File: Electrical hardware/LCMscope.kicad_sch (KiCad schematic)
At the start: 3 parts, among them U1 ICE40UP5K-SG48ITR, U2 LTC2299xUP, Y1 ASV-xxxMHz

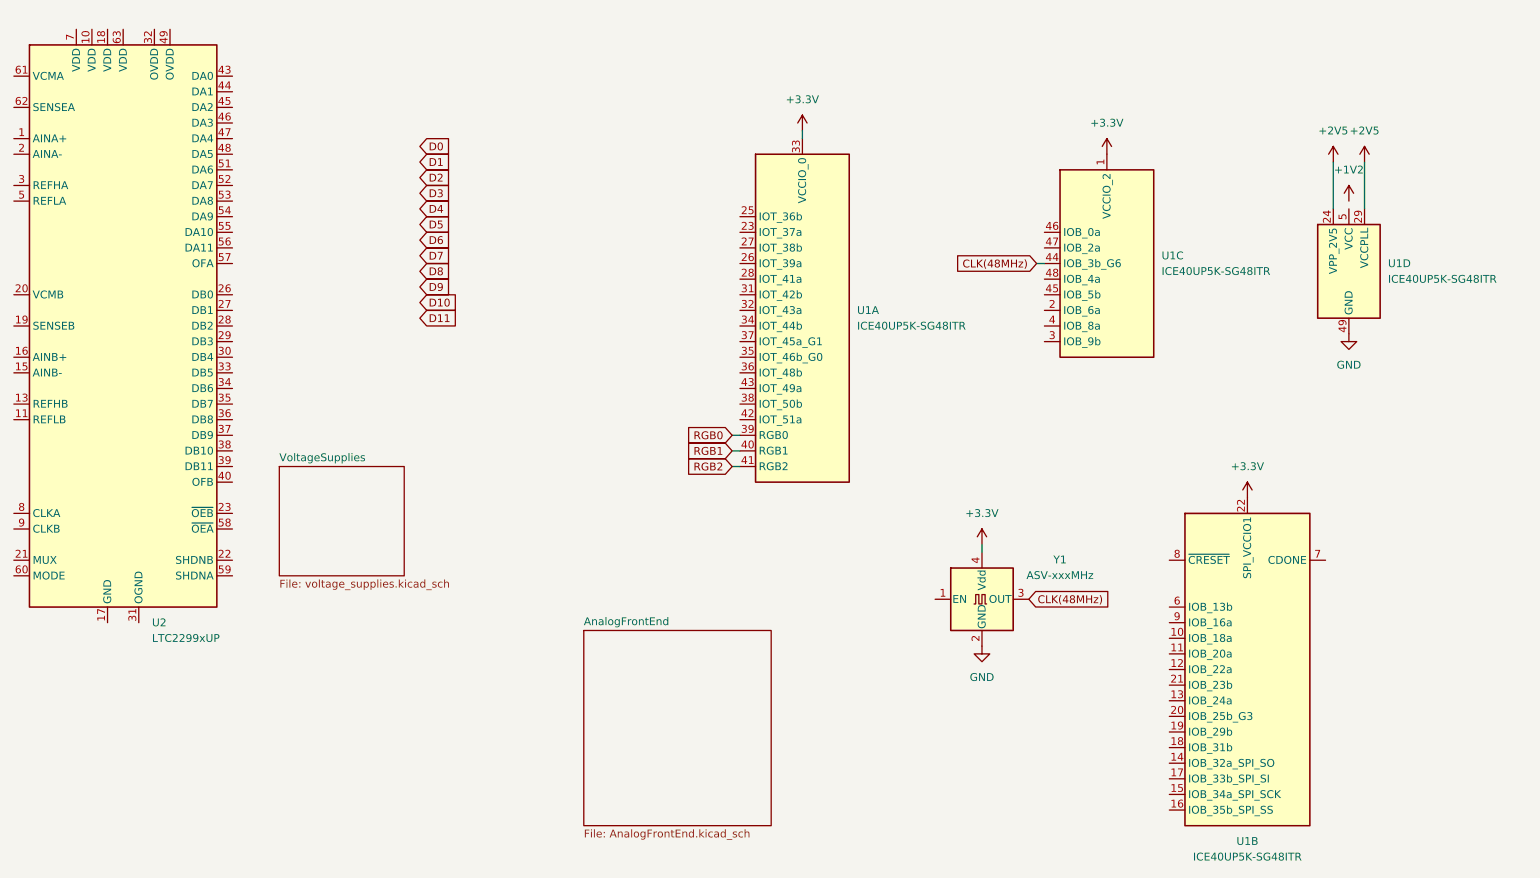
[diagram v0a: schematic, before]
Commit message: added hierarchical structure
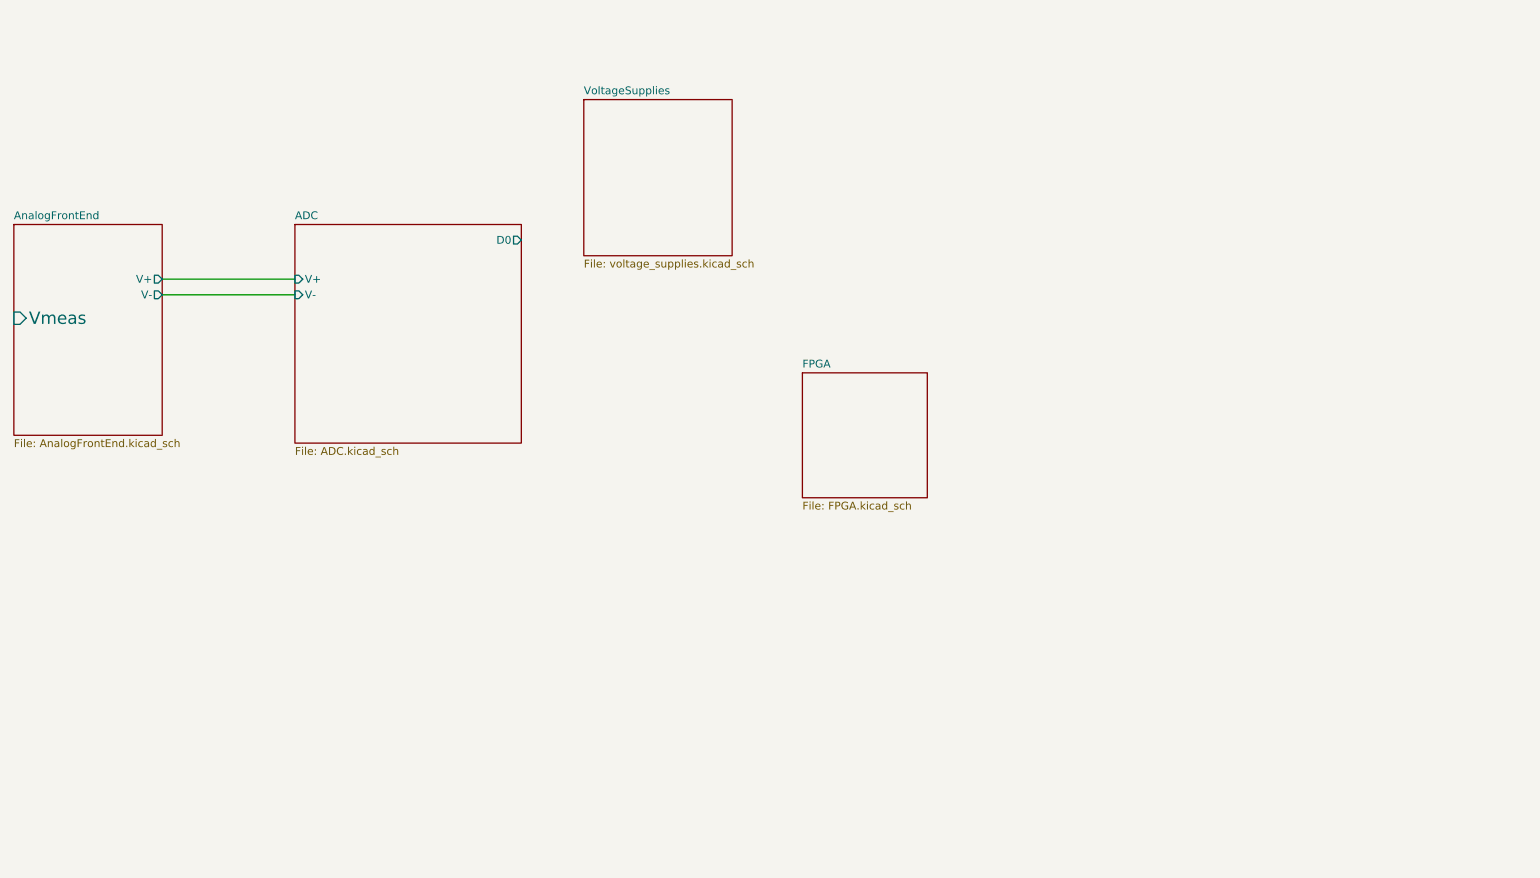
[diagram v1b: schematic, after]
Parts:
- removed U1: ICE40UP5K-SG48ITR, Package_DFN_QFN:QFN-48-1EP_7x7mm_P0.5mm_EP5.6x5.6mm, symbol FPGA_Lattice:ICE40UP5K-SG48ITR
- removed U2: LTC2299xUP, Package_DFN_QFN:QFN-64-1EP_9x9mm_P0.5mm_EP7.15x7.15mm, symbol Analog_ADC:LTC2299xUP
- removed Y1: ASV-xxxMHz, Oscillator:Oscillator_SMD_Abracon_ASV-4Pin_7.0x5.1mm, symbol Oscillator:ASV-xxxMHz
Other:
- added sheet ADC (ADC.kicad_sch)
- added sheet FPGA (FPGA.kicad_sch)
- sheet AnalogFrontEnd ports: added V+, V-, Vmeas; removed none

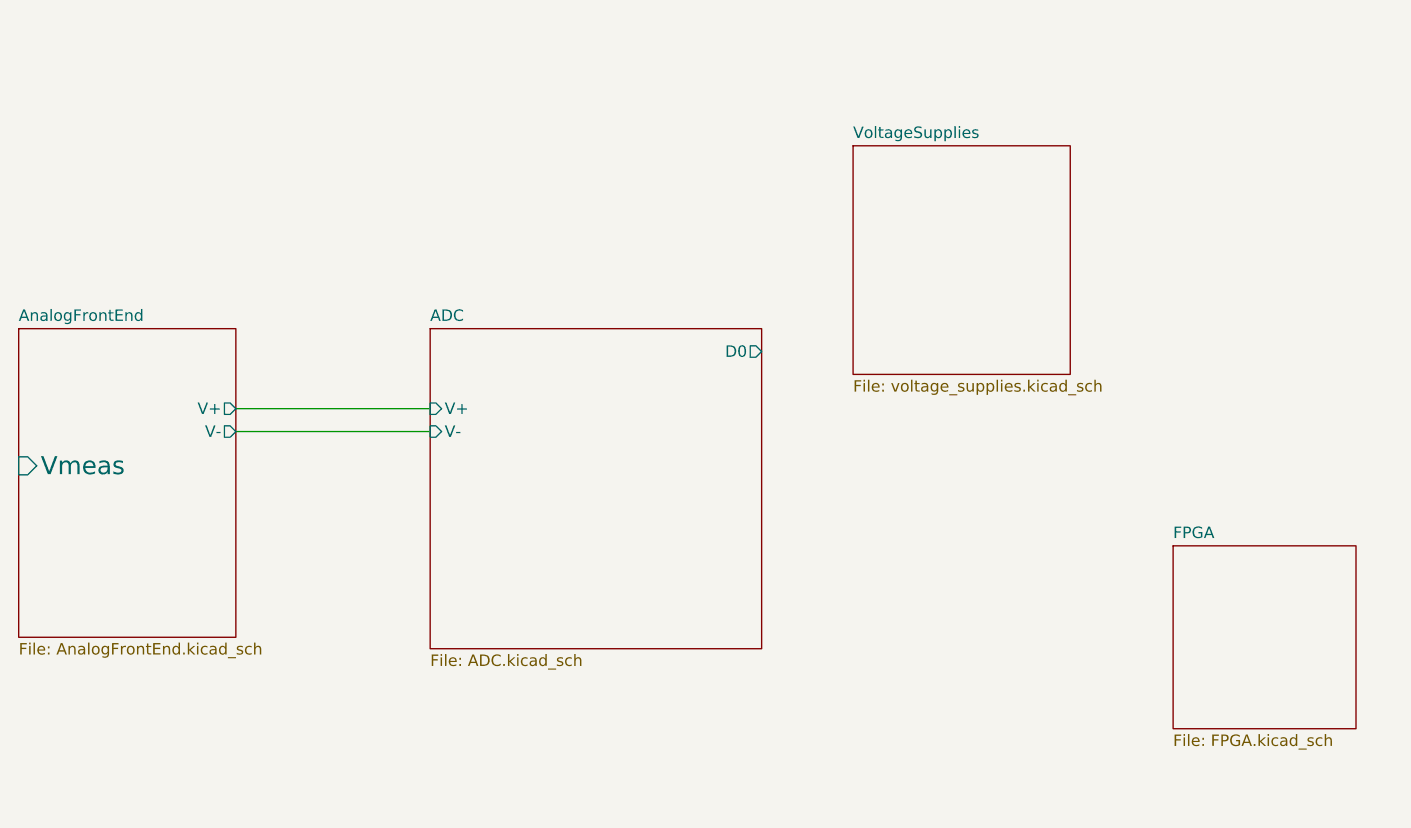
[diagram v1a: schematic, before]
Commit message: Created ADC footprint and extracted most important data from the data sheet
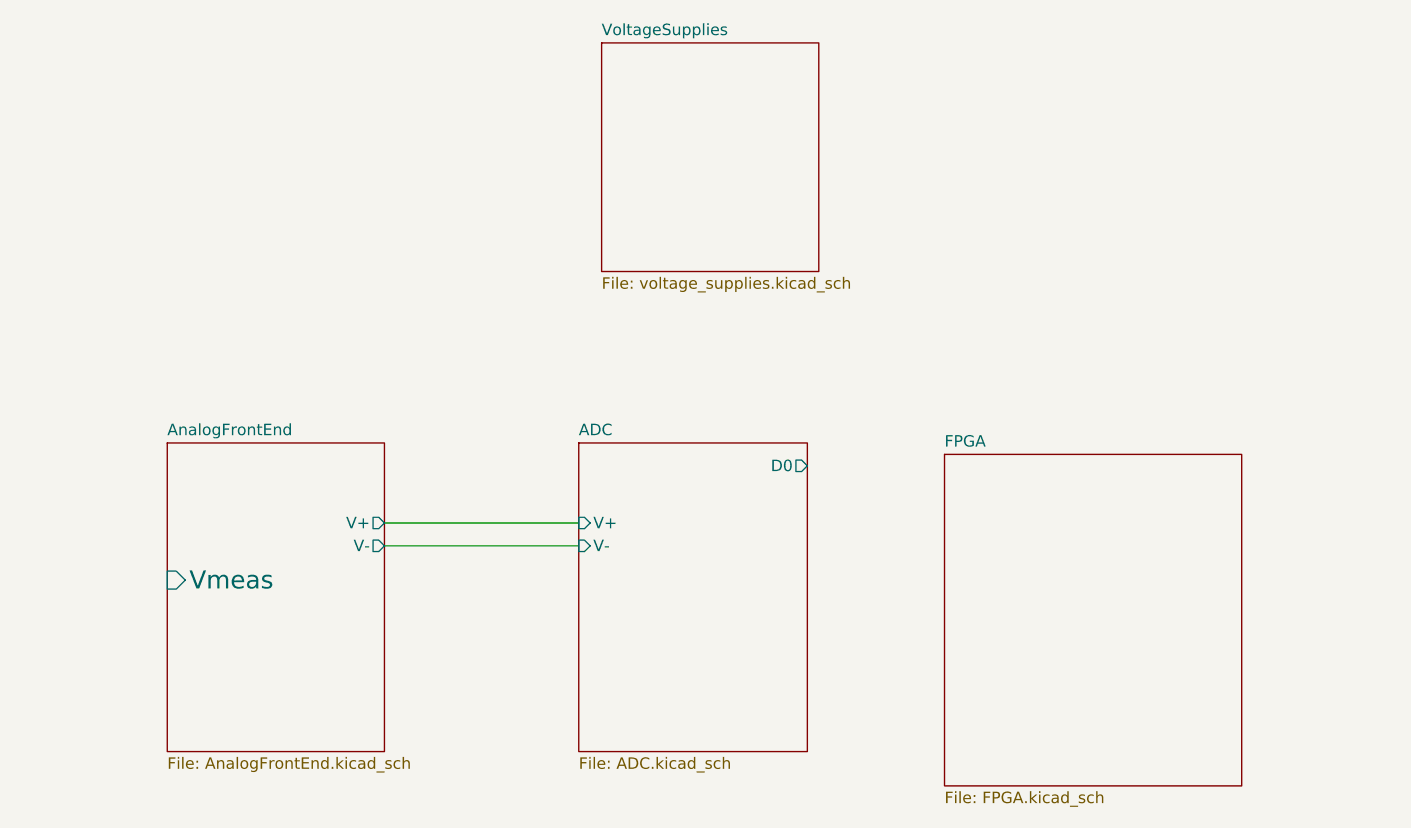
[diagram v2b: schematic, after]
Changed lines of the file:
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@@
 	(wire
 		(pts
-			(xy 64.77 55.88) (xy 86.36 55.88)
+			(xy 81.28 68.58) (xy 102.87 68.58)
 		)
 		(stroke
@@
 	(wire
 		(pts
-			(xy 64.77 58.42) (xy 86.36 58.42)
+			(xy 81.28 71.12) (xy 102.87 71.12)
 		)
 		(stroke
@@
 	)
 	(sheet
-		(at 40.64 46.99)
+		(at 57.15 59.69)
 		(size 24.13 34.29)
 		(exclude_from_sim no)
@@
 		)
 		(fill
-			(color 0 0 0 0.0000)
+			(color 255 194 1 1.0000)
 		)
 		(property "Sheetname" "AnalogFrontEnd"
-			(at 40.64 46.2784 0)
+			(at 57.15 58.9784 0)
 			(effects
 				(font
@@
 		)
 		(property "Sheetfile" "AnalogFrontEnd.kicad_sch"
-			(at 40.64 81.8646 0)
+			(at 57.15 94.5646 0)
 			(effects
 				(font
@@
 		)
 		(pin "V+" output
-			(at 64.77 55.88 0)
+			(at 81.28 68.58 0)
 			(effects
 				(font
@@
 		)
 		(pin "V-" output
-			(at 64.77 58.42 0)
+			(at 81.28 71.12 0)
 			(effects
 				(font
@@
 		)
 		(pin "Vmeas" input
-			(at 40.64 62.23 180)
+			(at 57.15 74.93 180)
 			(effects
 				(font
@@
 	)
 	(sheet
-		(at 86.36 46.99)
-		(size 36.83 35.56)
-		(exclude_from_sim no)
-		(in_bom yes)
-		(on_board yes)
-		(dnp no)
-		(fields_autoplaced yes)
-		(stroke
-			(width 0.1524)
-			(type solid)
-		)
-		(fill
-			(color 0 0 0 0.0000)
+		(at 102.87 59.69)
+		(size 25.4 34.29)
+		(exclude_from_sim no)
+		(in_bom yes)
+		(on_board yes)
+		(dnp no)
+		(fields_autoplaced yes)
+		(stroke
+			(width 0.1524)
+			(type solid)
+		)
+		(fill
+			(color 122 255 112 1.0000)
 		)
 		(property "Sheetname" "ADC"
-			(at 86.36 46.2784 0)
+			(at 102.87 58.9784 0)
 			(effects
 				(font
@@
 		)
 		(property "Sheetfile" "ADC.kicad_sch"
-			(at 86.36 83.1346 0)
+			(at 102.87 94.5646 0)
 			(effects
 				(font
@@
 		)
 		(pin "D0" output
-			(at 123.19 49.53 0)
+			(at 128.27 62.23 0)
 			(effects
 				(font
@@
 		)
 		(pin "V+" input
-			(at 86.36 55.88 180)
+			(at 102.87 68.58 180)
 			(effects
 				(font
@@
 		)
 		(pin "V-" input
-			(at 86.36 58.42 180)
+			(at 102.87 71.12 180)
 			(effects
 				(font
@@
 	)
 	(sheet
-		(at 133.35 26.67)
+		(at 105.41 15.24)
 		(size 24.13 25.4)
 		(exclude_from_sim no)
@@
 		)
 		(property "Sheetname" "VoltageSupplies"
-			(at 133.35 25.9584 0)
+			(at 105.41 14.5284 0)
 			(effects
 				(font
@@
 		)
 		(property "Sheetfile" "voltage_supplies.kicad_sch"
-			(at 133.35 52.6546 0)
+			(at 105.41 41.2246 0)
 			(effects
 				(font
@@
 	)
 	(sheet
-		(at 168.91 71.12)
-		(size 20.32 20.32)
-		(exclude_from_sim no)
-		(in_bom yes)
-		(on_board yes)
-		(dnp no)
-		(fields_autoplaced yes)
-		(stroke
-			(width 0.1524)
-			(type solid)
-		)
-		(fill
-			(color 0 0 0 0.0000)
+		(at 143.51 60.96)
+		(size 33.02 36.83)
+		(exclude_from_sim no)
+		(in_bom yes)
+		(on_board yes)
+		(dnp no)
+		(fields_autoplaced yes)
+		(stroke
+			(width 0.1524)
+			(type solid)
+		)
+		(fill
+			(color 101 220 255 1.0000)
 		)
 		(property "Sheetname" "FPGA"
-			(at 168.91 70.4084 0)
+			(at 143.51 60.2484 0)
 			(effects
 				(font
@@
 		)
 		(property "Sheetfile" "FPGA.kicad_sch"
-			(at 168.91 92.0246 0)
+			(at 143.51 98.3746 0)
 			(effects
 				(font
@@
 		)
 		(property "Field2" ""
-			(at 168.91 71.12 0)
-			(effects
-				(font
+			(at 143.51 60.96 0)
+			(effects
+				(font
